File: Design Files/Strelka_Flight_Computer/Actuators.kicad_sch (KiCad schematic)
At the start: 15 parts

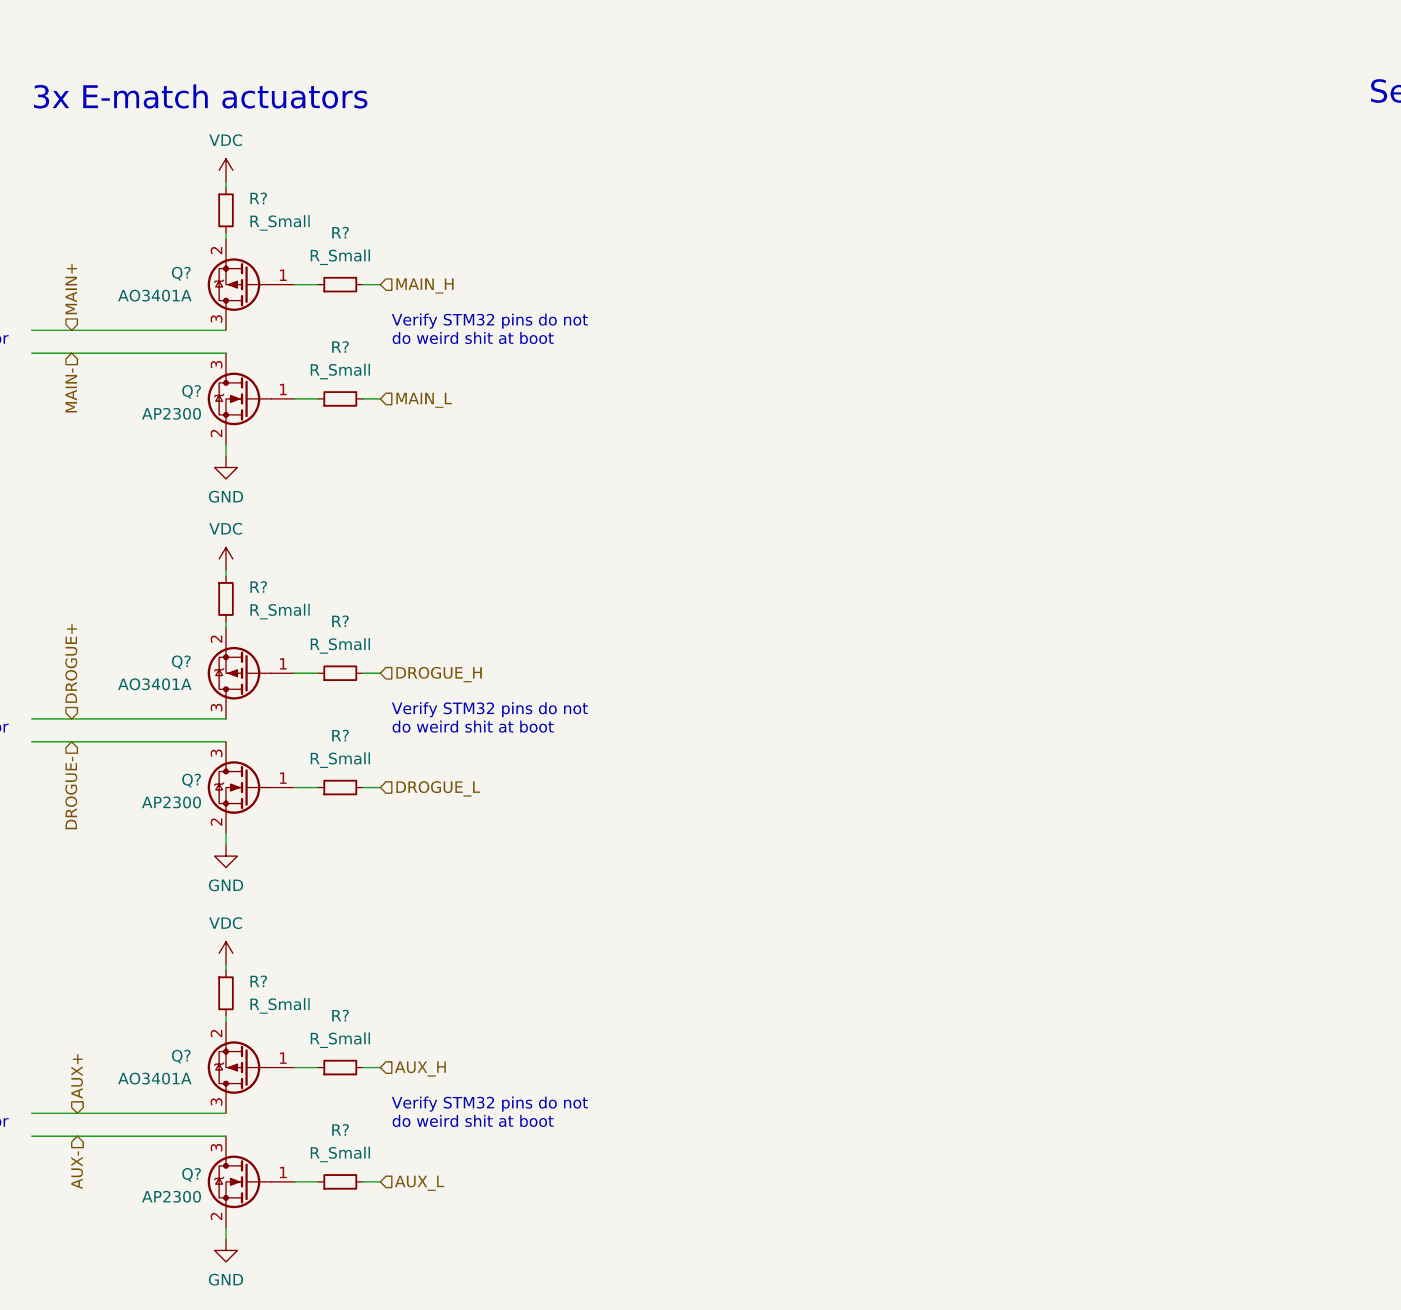
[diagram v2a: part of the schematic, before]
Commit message: Working SPICE sim for ematch continuity circuit
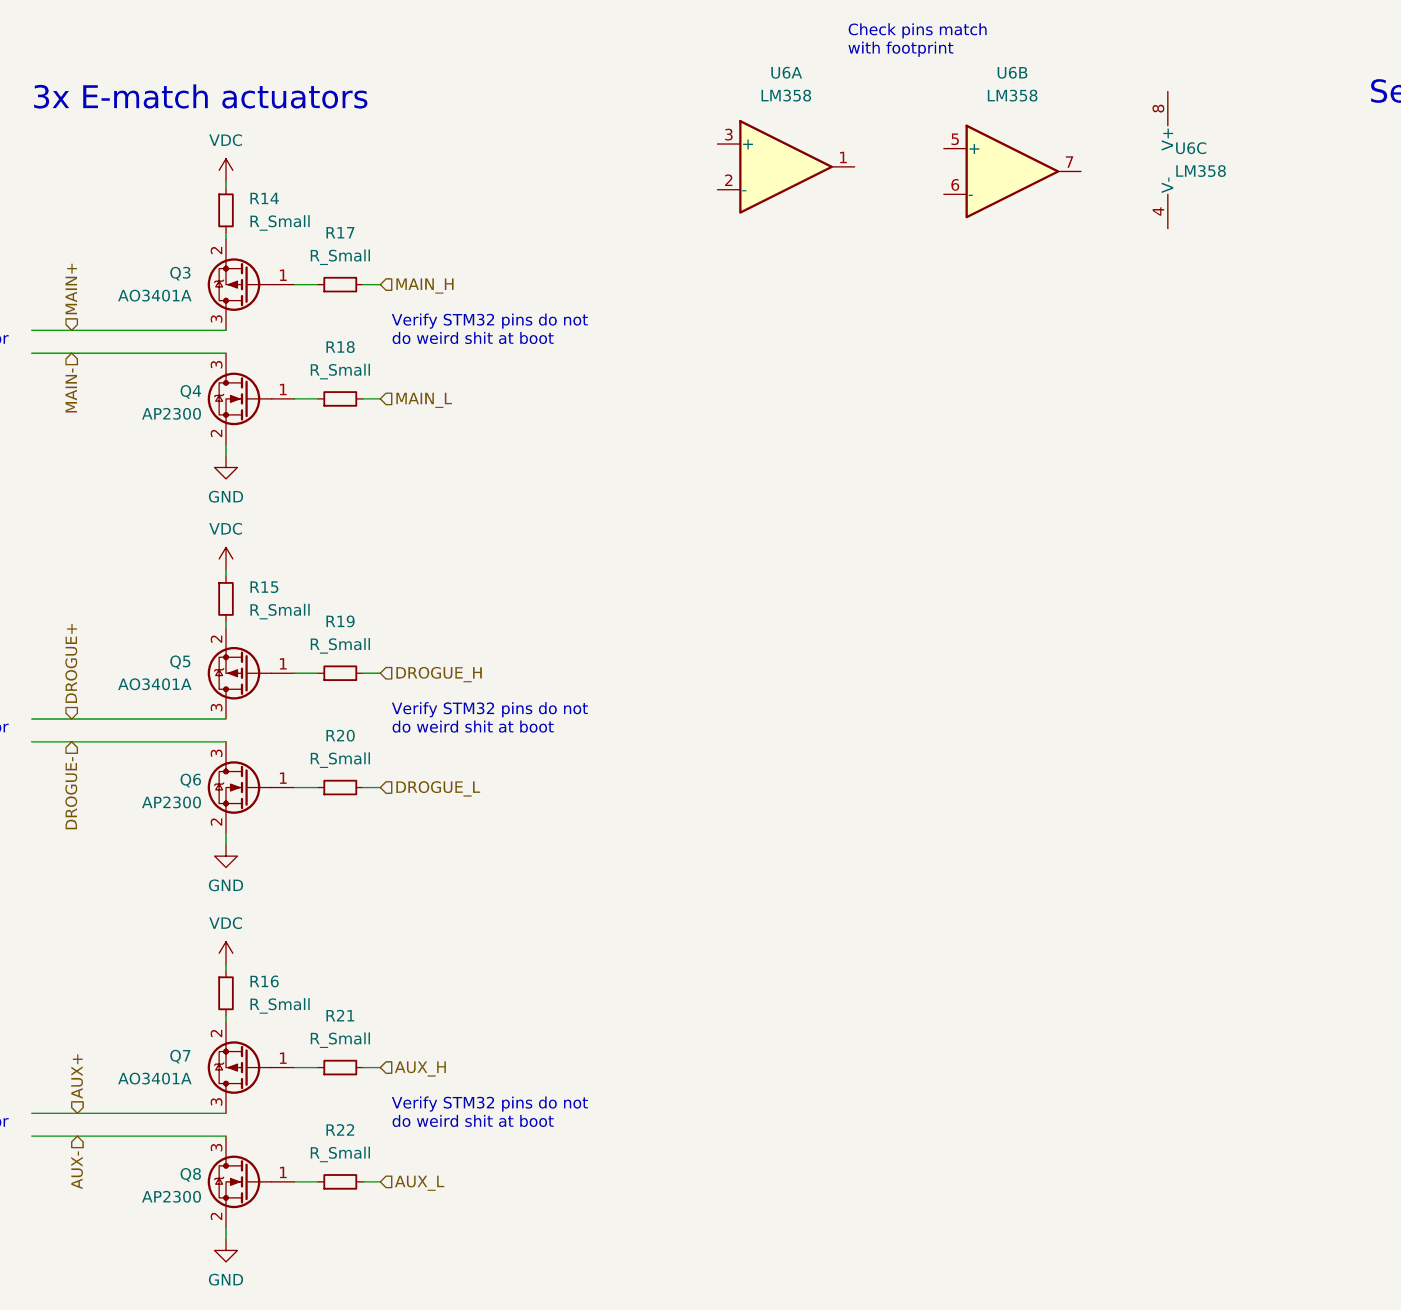
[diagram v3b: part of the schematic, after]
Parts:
- added U6: LM358, Footprints:SOP65P490X110-8N, symbol Amplifier_Operational:LM358
- gave numbers to parts that had none: 15
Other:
- note added: "Check pins match with footprint"
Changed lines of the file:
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@@
+    (effects (font (size 1.27 1.27)) (justify left bottom))
+  )
+  (text "Check pins match\nwith footprint" (at 136.398 38.862 0)
     (effects (font (size 1.27 1.27)) (justify left bottom))
   )
@@
   (symbol (lib_id "Transistor_FET:AO3401A") (at 69.85 64.135 180) (unit 1)
     (in_bom yes) (on_board yes) (fields_autoplaced)
-    (property "Reference" "Q?" (id 0) (at 63.5 62.8649 0)
+    (property "Reference" "Q3" (id 0) (at 63.5 62.8649 0)
       (effects (font (size 1.27 1.27)) (justify left))
     )
@@
   (symbol (lib_id "Device:R_Small") (at 67.31 142.875 0) (unit 1)
     (in_bom yes) (on_board yes) (fields_autoplaced)
-    (property "Reference" "R?" (id 0) (at 69.85 141.6049 0)
+    (property "Reference" "R16" (id 0) (at 69.85 141.6049 0)
       (effects (font (size 1.27 1.27)) (justify left))
     )
@@
   (symbol (lib_id "Device:R_Small") (at 80.01 151.13 90) (unit 1)
     (in_bom yes) (on_board yes) (fields_autoplaced)
-    (property "Reference" "R?" (id 0) (at 80.01 145.415 90))
+    (property "Reference" "R21" (id 0) (at 80.01 145.415 90))
     (property "Value" "R_Small" (id 1) (at 80.01 147.955 90))
     (property "Footprint" "" (id 2) (at 80.01 151.13 0)
@@
   (symbol (lib_id "power:GND") (at 67.31 83.185 0) (unit 1)
     (in_bom yes) (on_board yes) (fields_autoplaced)
-    (property "Reference" "#PWR?" (id 0) (at 67.31 89.535 0)
+    (property "Reference" "#PWR0141" (id 0) (at 67.31 89.535 0)
       (effects (font (size 1.27 1.27)) hide)
     )
@@
   (symbol (lib_id "Transistor_FET:AO3401A") (at 69.85 151.13 180) (unit 1)
     (in_bom yes) (on_board yes) (fields_autoplaced)
-    (property "Reference" "Q?" (id 0) (at 63.5 149.8599 0)
+    (property "Reference" "Q7" (id 0) (at 63.5 149.8599 0)
       (effects (font (size 1.27 1.27)) (justify left))
     )
@@
   (symbol (lib_id "power:VDC") (at 67.31 139.7 0) (unit 1)
     (in_bom yes) (on_board yes) (fields_autoplaced)
-    (property "Reference" "#PWR?" (id 0) (at 67.31 142.24 0)
+    (property "Reference" "#PWR0142" (id 0) (at 67.31 142.24 0)
       (effects (font (size 1.27 1.27)) hide)
     )
@@
   (symbol (lib_id "Transistor_FET:2N7002E") (at 69.85 120.015 0) (mirror y) (unit 1)
     (in_bom yes) (on_board yes) (fields_autoplaced)
-    (property "Reference" "Q?" (id 0) (at 64.6431 119.1803 0)
+    (property "Reference" "Q6" (id 0) (at 64.6431 119.1803 0)
       (effects (font (size 1.27 1.27)) (justify left))
     )
@@
   (symbol (lib_id "power:VDC") (at 67.31 52.705 0) (unit 1)
     (in_bom yes) (on_board yes) (fields_autoplaced)
-    (property "Reference" "#PWR?" (id 0) (at 67.31 55.245 0)
+    (property "Reference" "#PWR0146" (id 0) (at 67.31 55.245 0)
       (effects (font (size 1.27 1.27)) hide)
     )
@@
   (symbol (lib_id "Device:R_Small") (at 80.01 64.135 90) (unit 1)
     (in_bom yes) (on_board yes) (fields_autoplaced)
-    (property "Reference" "R?" (id 0) (at 80.01 58.42 90))
+    (property "Reference" "R17" (id 0) (at 80.01 58.42 90))
     (property "Value" "R_Small" (id 1) (at 80.01 60.96 90))
     (property "Footprint" "" (id 2) (at 80.01 64.135 0)
@@
   (symbol (lib_id "Transistor_FET:AO3401A") (at 69.85 107.315 180) (unit 1)
     (in_bom yes) (on_board yes) (fields_autoplaced)
-    (property "Reference" "Q?" (id 0) (at 63.5 106.0449 0)
+    (property "Reference" "Q5" (id 0) (at 63.5 106.0449 0)
       (effects (font (size 1.27 1.27)) (justify left))
     )
@@
   (symbol (lib_id "Device:R_Small") (at 67.31 55.88 0) (unit 1)
     (in_bom yes) (on_board yes) (fields_autoplaced)
-    (property "Reference" "R?" (id 0) (at 69.85 54.6099 0)
+    (property "Reference" "R14" (id 0) (at 69.85 54.6099 0)
       (effects (font (size 1.27 1.27)) (justify left))
     )
@@
   (symbol (lib_id "Device:R_Small") (at 80.01 76.835 90) (unit 1)
     (in_bom yes) (on_board yes) (fields_autoplaced)
-    (property "Reference" "R?" (id 0) (at 80.01 71.12 90))
+    (property "Reference" "R18" (id 0) (at 80.01 71.12 90))
     (property "Value" "R_Small" (id 1) (at 80.01 73.66 90))
     (property "Footprint" "" (id 2) (at 80.01 76.835 0)
@@
   (symbol (lib_id "Device:R_Small") (at 80.01 107.315 90) (unit 1)
     (in_bom yes) (on_board yes) (fields_autoplaced)
-    (property "Reference" "R?" (id 0) (at 80.01 101.6 90))
+    (property "Reference" "R19" (id 0) (at 80.01 101.6 90))
     (property "Value" "R_Small" (id 1) (at 80.01 104.14 90))
     (property "Footprint" "" (id 2) (at 80.01 107.315 0)
@@
   (symbol (lib_id "power:GND") (at 67.31 126.365 0) (unit 1)
     (in_bom yes) (on_board yes) (fields_autoplaced)
-    (property "Reference" "#PWR?" (id 0) (at 67.31 132.715 0)
+    (property "Reference" "#PWR0143" (id 0) (at 67.31 132.715 0)
       (effects (font (size 1.27 1.27)) hide)
     )
@@
     (pin "1")
   )
+  (symbol (lib_id "Amplifier_Operational:LM358") (at 129.54 51.054 0) (unit 1)
+    (in_bom yes) (on_board yes) (fields_autoplaced)
+    (property "Reference" "U6" (id 0) (at 129.54 40.64 0))
+    (property "Value" "LM358" (id 1) (at 129.54 43.18 0))
+    (property "Footprint" "Footprints:SOP65P490X110-8N" (id 2) (at 129.54 51.054 0)
+      (effects (font (size 1.27 1.27)) hide)
+    )
+    (property "Datasheet" "http://www.ti.com/lit/ds/symlink/lm2904-n.pdf" (id 3) (at 129.54 51.054 0)
+      (effects (font (size 1.27 1.27)) hide)
+    )
+    (pin "1")
+    (pin "2")
+    (pin "3")
+  )
   (symbol (lib_id "Transistor_FET:2N7002E") (at 69.85 163.83 0) (mirror y) (unit 1)
     (in_bom yes) (on_board yes) (fields_autoplaced)
-    (property "Reference" "Q?" (id 0) (at 64.6431 162.9953 0)
+    (property "Reference" "Q8" (id 0) (at 64.6431 162.9953 0)
       (effects (font (size 1.27 1.27)) (justify left))
     )
@@
   (symbol (lib_id "power:GND") (at 67.31 170.18 0) (unit 1)
     (in_bom yes) (on_board yes) (fields_autoplaced)
-    (property "Reference" "#PWR?" (id 0) (at 67.31 176.53 0)
+    (property "Reference" "#PWR0145" (id 0) (at 67.31 176.53 0)
       (effects (font (size 1.27 1.27)) hide)
     )
@@
   (symbol (lib_id "Device:R_Small") (at 80.01 120.015 90) (unit 1)
     (in_bom yes) (on_board yes) (fields_autoplaced)
-    (property "Reference" "R?" (id 0) (at 80.01 114.3 90))
+    (property "Reference" "R20" (id 0) (at 80.01 114.3 90))
     (property "Value" "R_Small" (id 1) (at 80.01 116.84 90))
     (property "Footprint" "" (id 2) (at 80.01 120.015 0)
@@
   (symbol (lib_id "Transistor_FET:2N7002E") (at 69.85 76.835 0) (mirror y) (unit 1)
     (in_bom yes) (on_board yes) (fields_autoplaced)
-    (property "Reference" "Q?" (id 0) (at 64.6431 76.0003 0)
+    (property "Reference" "Q4" (id 0) (at 64.6431 76.0003 0)
       (effects (font (size 1.27 1.27)) (justify left))
     )
@@
     (pin "3")
   )
+  (symbol (lib_id "Amplifier_Operational:LM358") (at 154.686 51.562 0) (unit 2)
+    (in_bom yes) (on_board yes) (fields_autoplaced)
+    (property "Reference" "U6" (id 0) (at 154.686 40.64 0))
+    (property "Value" "LM358" (id 1) (at 154.686 43.18 0))
+    (property "Footprint" "" (id 2) (at 154.686 51.562 0)
+      (effects (font (size 1.27 1.27)) hide)
+    )
+    (property "Datasheet" "http://www.ti.com/lit/ds/symlink/lm2904-n.pdf" (id 3) (at 154.686 51.562 0)
+      (effects (font (size 1.27 1.27)) hide)
+    )
+    (pin "5")
+    (pin "6")
+    (pin "7")
+  )
   (symbol (lib_id "Device:R_Small") (at 80.01 163.83 90) (unit 1)
     (in_bom yes) (on_board yes) (fields_autoplaced)
-    (property "Reference" "R?" (id 0) (at 80.01 158.115 90))
+    (property "Reference" "R22" (id 0) (at 80.01 158.115 90))
     (property "Value" "R_Small" (id 1) (at 80.01 160.655 90))
     (property "Footprint" "" (id 2) (at 80.01 163.83 0)
@@
   (symbol (lib_id "Device:R_Small") (at 67.31 99.06 0) (unit 1)
     (in_bom yes) (on_board yes) (fields_autoplaced)
-    (property "Reference" "R?" (id 0) (at 69.85 97.7899 0)
+    (property "Reference" "R15" (id 0) (at 69.85 97.7899 0)
       (effects (font (size 1.27 1.27)) (justify left))
     )
@@
     (pin "2")
   )
+  (symbol (lib_id "Amplifier_Operational:LM358") (at 174.498 50.292 0) (unit 3)
+    (in_bom yes) (on_board yes) (fields_autoplaced)
+    (property "Reference" "U6" (id 0) (at 172.72 49.0219 0)
+      (effects (font (size 1.27 1.27)) (justify left))
+    )
+    (property "Value" "LM358" (id 1) (at 172.72 51.5619 0)
+      (effects (font (size 1.27 1.27)) (justify left))
+    )
+    (property "Footprint" "" (id 2) (at 174.498 50.292 0)
+      (effects (font (size 1.27 1.27)) hide)
+    )
+    (property "Datasheet" "http://www.ti.com/lit/ds/symlink/lm2904-n.pdf" (id 3) (at 174.498 50.292 0)
+      (effects (font (size 1.27 1.27)) hide)
+    )
+    (pin "4")
+    (pin "8")
+  )
   (symbol (lib_id "power:VDC") (at 67.31 95.885 0) (unit 1)
     (in_bom yes) (on_board yes) (fields_autoplaced)
-    (property "Reference" "#PWR?" (id 0) (at 67.31 98.425 0)
-      (effects (font (size 1.27 1.27)) hide)
-    )
+    (property "Reference" "#PWR0144" (id 0) (at 67.31 98.425 0)
+      (effects (font (size 1.27 1.27)) hide)
+    )
